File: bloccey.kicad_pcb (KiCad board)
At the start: 2 copper layers, 12 parts

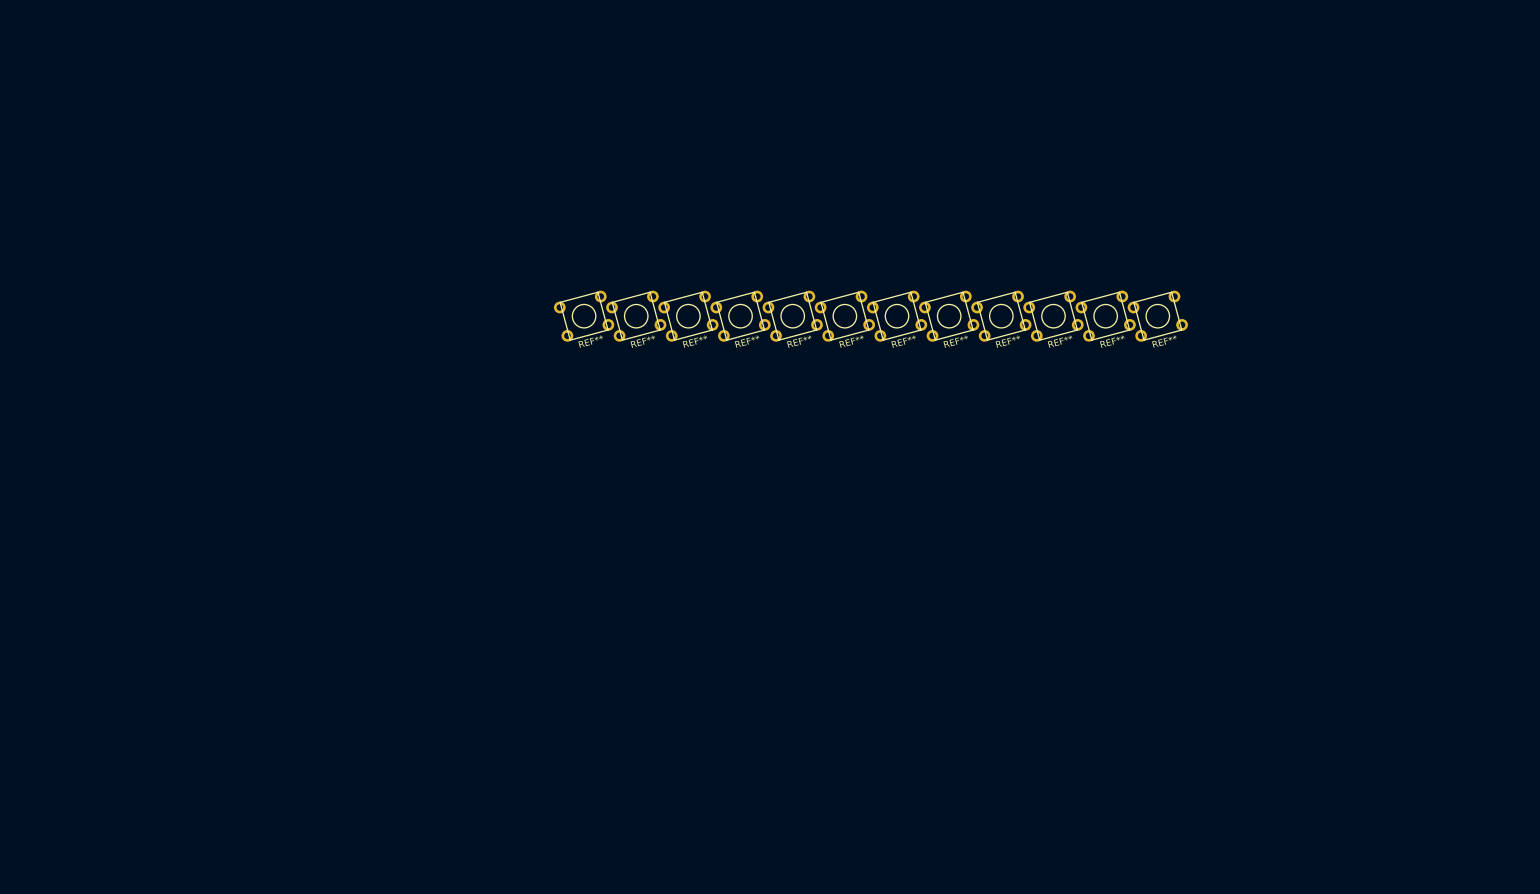
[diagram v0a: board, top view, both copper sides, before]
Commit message: Start of PCB layout, finished sch
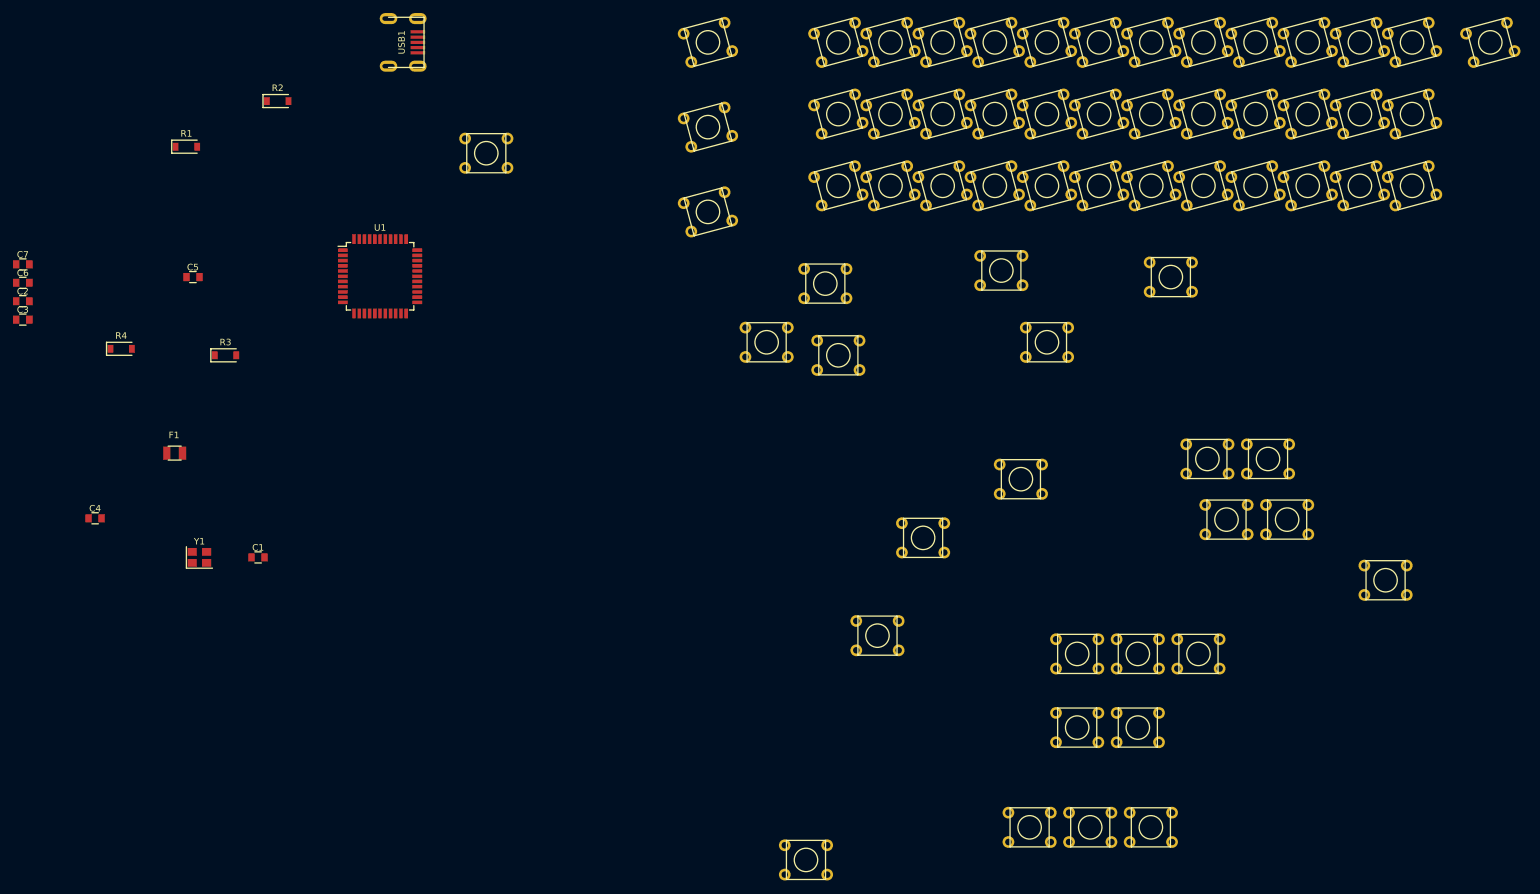
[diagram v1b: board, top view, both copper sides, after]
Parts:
- removed REF** (x12): PushButton_6x6mm_TH, random-keyboard-parts:PushButton_6x6mm_TH
- added C1: 22pF, Capacitors_SMD:C_0805, F.Cu at (61.0, 109.0)
- added C2: 22pF, Capacitors_SMD:C_0805, F.Cu at (24.9, 69.7)
- added C3: 1uF, Capacitors_SMD:C_0805, F.Cu at (24.9, 72.5)
- added C4: 0.1uF, Capacitors_SMD:C_0805, F.Cu at (36.0, 103.0)
- added C5: 0.1uF, Capacitors_SMD:C_0805, F.Cu at (51.0, 66.0)
- added C6: 0.1uF, Capacitors_SMD:C_0805, F.Cu at (24.9, 66.9)
- added C7: 10uF, Capacitors_SMD:C_0805, F.Cu at (24.9, 64.1)
- added F1: 500mA, Fuse_Holders_and_Fuses:Fuse_SMD1206_Reflow, F.Cu at (48.2, 93.0)
- added R1: 10k, random-keyboard-parts:D_SOD-123-Pretty, F.Cu at (50.0, 46.0)
- added R2: 22, random-keyboard-parts:D_SOD-123-Pretty, F.Cu at (64.0, 39.0)
- added R3: 22, random-keyboard-parts:D_SOD-123-Pretty, F.Cu at (56.0, 78.0)
- added R4: 10k, random-keyboard-parts:D_SOD-123-Pretty, F.Cu at (40.0, 77.0)
- added SW1: SW_Push, random-keyboard-parts:PushButton_6x6mm_TH_Pretty, F.Cu at (96.0, 47.0)
- added SW10: SW_Push, random-keyboard-parts:PushButton_6x6mm_TH_Pretty, F.Cu at (206.0, 30.0)
- added SW11: SW_Push, random-keyboard-parts:PushButton_6x6mm_TH_Pretty, F.Cu at (214.0, 30.0)
- added SW12: SW_Push, random-keyboard-parts:PushButton_6x6mm_TH_Pretty, F.Cu at (222.0, 30.0)
- added SW13: SW_Push, random-keyboard-parts:PushButton_6x6mm_TH_Pretty, F.Cu at (230.0, 30.0)
- added SW14: SW_Push, random-keyboard-parts:PushButton_6x6mm_TH_Pretty, F.Cu at (238.0, 30.0)
- added SW15: SW_Push, random-keyboard-parts:PushButton_6x6mm_TH_Pretty, F.Cu at (130.0, 43.0)
- added SW16: SW_Push, random-keyboard-parts:PushButton_6x6mm_TH_Pretty, F.Cu at (150.0, 41.0)
- added SW17: SW_Push, random-keyboard-parts:PushButton_6x6mm_TH_Pretty, F.Cu at (158.0, 41.0)
- added SW18: SW_Push, random-keyboard-parts:PushButton_6x6mm_TH_Pretty, F.Cu at (166.0, 41.0)
- added SW19: SW_Push, random-keyboard-parts:PushButton_6x6mm_TH_Pretty, F.Cu at (174.0, 41.0)
- added SW2: SW_Push, random-keyboard-parts:PushButton_6x6mm_TH_Pretty, F.Cu at (130.0, 30.0)
- added SW20: SW_Push, random-keyboard-parts:PushButton_6x6mm_TH_Pretty, F.Cu at (182.0, 41.0)
- added SW21: SW_Push, random-keyboard-parts:PushButton_6x6mm_TH_Pretty, F.Cu at (190.0, 41.0)
- added SW22: SW_Push, random-keyboard-parts:PushButton_6x6mm_TH_Pretty, F.Cu at (198.0, 41.0)
- added SW23: SW_Push, random-keyboard-parts:PushButton_6x6mm_TH_Pretty, F.Cu at (206.0, 41.0)
- added SW24: SW_Push, random-keyboard-parts:PushButton_6x6mm_TH_Pretty, F.Cu at (214.0, 41.0)
- added SW25: SW_Push, random-keyboard-parts:PushButton_6x6mm_TH_Pretty, F.Cu at (222.0, 41.0)
- added SW26: SW_Push, random-keyboard-parts:PushButton_6x6mm_TH_Pretty, F.Cu at (230.0, 41.0)
- added SW27: SW_Push, random-keyboard-parts:PushButton_6x6mm_TH_Pretty, F.Cu at (238.0, 41.0)
- added SW28: SW_Push, random-keyboard-parts:PushButton_6x6mm_TH_Pretty, F.Cu at (130.0, 56.0)
- added SW29: SW_Push, random-keyboard-parts:PushButton_6x6mm_TH_Pretty, F.Cu at (150.0, 52.0)
- added SW3: SW_Push, random-keyboard-parts:PushButton_6x6mm_TH_Pretty, F.Cu at (150.0, 30.0)
- added SW30: SW_Push, random-keyboard-parts:PushButton_6x6mm_TH_Pretty, F.Cu at (158.0, 52.0)
- added SW31: SW_Push, random-keyboard-parts:PushButton_6x6mm_TH_Pretty, F.Cu at (166.0, 52.0)
- added SW32: SW_Push, random-keyboard-parts:PushButton_6x6mm_TH_Pretty, F.Cu at (174.0, 52.0)
- added SW33: SW_Push, random-keyboard-parts:PushButton_6x6mm_TH_Pretty, F.Cu at (182.0, 52.0)
- added SW34: SW_Push, random-keyboard-parts:PushButton_6x6mm_TH_Pretty, F.Cu at (190.0, 52.0)
- added SW35: SW_Push, random-keyboard-parts:PushButton_6x6mm_TH_Pretty, F.Cu at (198.0, 52.0)
- added SW36: SW_Push, random-keyboard-parts:PushButton_6x6mm_TH_Pretty, F.Cu at (206.0, 52.0)
- added SW37: SW_Push, random-keyboard-parts:PushButton_6x6mm_TH_Pretty, F.Cu at (214.0, 52.0)
- added SW38: SW_Push, random-keyboard-parts:PushButton_6x6mm_TH_Pretty, F.Cu at (222.0, 52.0)
- added SW39: SW_Push, random-keyboard-parts:PushButton_6x6mm_TH_Pretty, F.Cu at (230.0, 52.0)
- added SW4: SW_Push, random-keyboard-parts:PushButton_6x6mm_TH_Pretty, F.Cu at (158.0, 30.0)
- added SW40: SW_Push, random-keyboard-parts:PushButton_6x6mm_TH_Pretty, F.Cu at (238.0, 52.0)
- added SW41: SW_Push, random-keyboard-parts:PushButton_6x6mm_TH_Pretty, F.Cu at (186.6, 123.8)
- added SW42: SW_Push, random-keyboard-parts:PushButton_6x6mm_TH_Pretty, F.Cu at (233.9, 112.5)
- added SW43: SW_Push, random-keyboard-parts:PushButton_6x6mm_TH_Pretty, F.Cu at (148.0, 67.0)
- added SW44: SW_Push, random-keyboard-parts:PushButton_6x6mm_TH_Pretty, F.Cu at (178.0, 97.0)
- added SW45: SW_Push, random-keyboard-parts:PushButton_6x6mm_TH_Pretty, F.Cu at (175.0, 65.0)
- added SW46: SW_Push, random-keyboard-parts:PushButton_6x6mm_TH_Pretty, F.Cu at (179.3, 150.4)
- added SW47: SW_Push, random-keyboard-parts:PushButton_6x6mm_TH_Pretty, F.Cu at (215.9, 93.9)
- added SW48: SW_Push, random-keyboard-parts:PushButton_6x6mm_TH_Pretty, F.Cu at (145.0, 155.4)
- added SW49: SW_Push, random-keyboard-parts:PushButton_6x6mm_TH_Pretty, F.Cu at (201.0, 66.0)
- added SW5: SW_Push, random-keyboard-parts:PushButton_6x6mm_TH_Pretty, F.Cu at (166.0, 30.0)
- added SW50: SW_Push, random-keyboard-parts:PushButton_6x6mm_TH_Pretty, F.Cu at (163.0, 106.0)
- added SW51: SW_Push, random-keyboard-parts:PushButton_6x6mm_TH_Pretty, F.Cu at (156.0, 121.0)
- added SW52: SW_Push, random-keyboard-parts:PushButton_6x6mm_TH_Pretty, F.Cu at (195.9, 123.8)
- added SW53: SW_Push, random-keyboard-parts:PushButton_6x6mm_TH_Pretty, F.Cu at (206.6, 93.9)
- added SW54: SW_Push, random-keyboard-parts:PushButton_6x6mm_TH_Pretty, F.Cu at (139.0, 76.0)
- added SW55: SW_Push, random-keyboard-parts:PushButton_6x6mm_TH_Pretty, F.Cu at (150.0, 78.0)
- added SW56: SW_Push, random-keyboard-parts:PushButton_6x6mm_TH_Pretty, F.Cu at (209.5, 103.2)
- added SW57: SW_Push, random-keyboard-parts:PushButton_6x6mm_TH_Pretty, F.Cu at (188.6, 150.4)
- added SW58: SW_Push, random-keyboard-parts:PushButton_6x6mm_TH_Pretty, F.Cu at (182.0, 76.0)
- added SW59: SW_Push, random-keyboard-parts:PushButton_6x6mm_TH_Pretty, F.Cu at (195.9, 135.1)
- added SW6: SW_Push, random-keyboard-parts:PushButton_6x6mm_TH_Pretty, F.Cu at (174.0, 30.0)
- added SW60: SW_Push, random-keyboard-parts:PushButton_6x6mm_TH_Pretty, F.Cu at (205.2, 123.8)
- added SW61: SW_Push, random-keyboard-parts:PushButton_6x6mm_TH_Pretty, F.Cu at (250.0, 30.0)
- added SW62: SW_Push, random-keyboard-parts:PushButton_6x6mm_TH_Pretty, F.Cu at (218.8, 103.2)
- added SW63: SW_Push, random-keyboard-parts:PushButton_6x6mm_TH_Pretty, F.Cu at (186.6, 135.1)
- added SW64: SW_Push, random-keyboard-parts:PushButton_6x6mm_TH_Pretty, F.Cu at (197.9, 150.4)
- added SW7: SW_Push, random-keyboard-parts:PushButton_6x6mm_TH_Pretty, F.Cu at (182.0, 30.0)
- added SW8: SW_Push, random-keyboard-parts:PushButton_6x6mm_TH_Pretty, F.Cu at (190.0, 30.0)
- added SW9: SW_Push, random-keyboard-parts:PushButton_6x6mm_TH_Pretty, F.Cu at (198.0, 30.0)
- added U1: ATmega32U4-AU, Housings_QFP:TQFP-44_10x10mm_Pitch0.8mm, F.Cu at (79.7, 65.9)
- added USB1: Molex-0548190589, random-keyboard-parts:Molex-0548190589, F.Cu at (81.0, 30.0)
- added Y1: 16MHz, Crystals:Crystal_SMD_3225-4pin_3.2x2.5mm, F.Cu at (52.0, 109.0)

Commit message: Updated switch positions
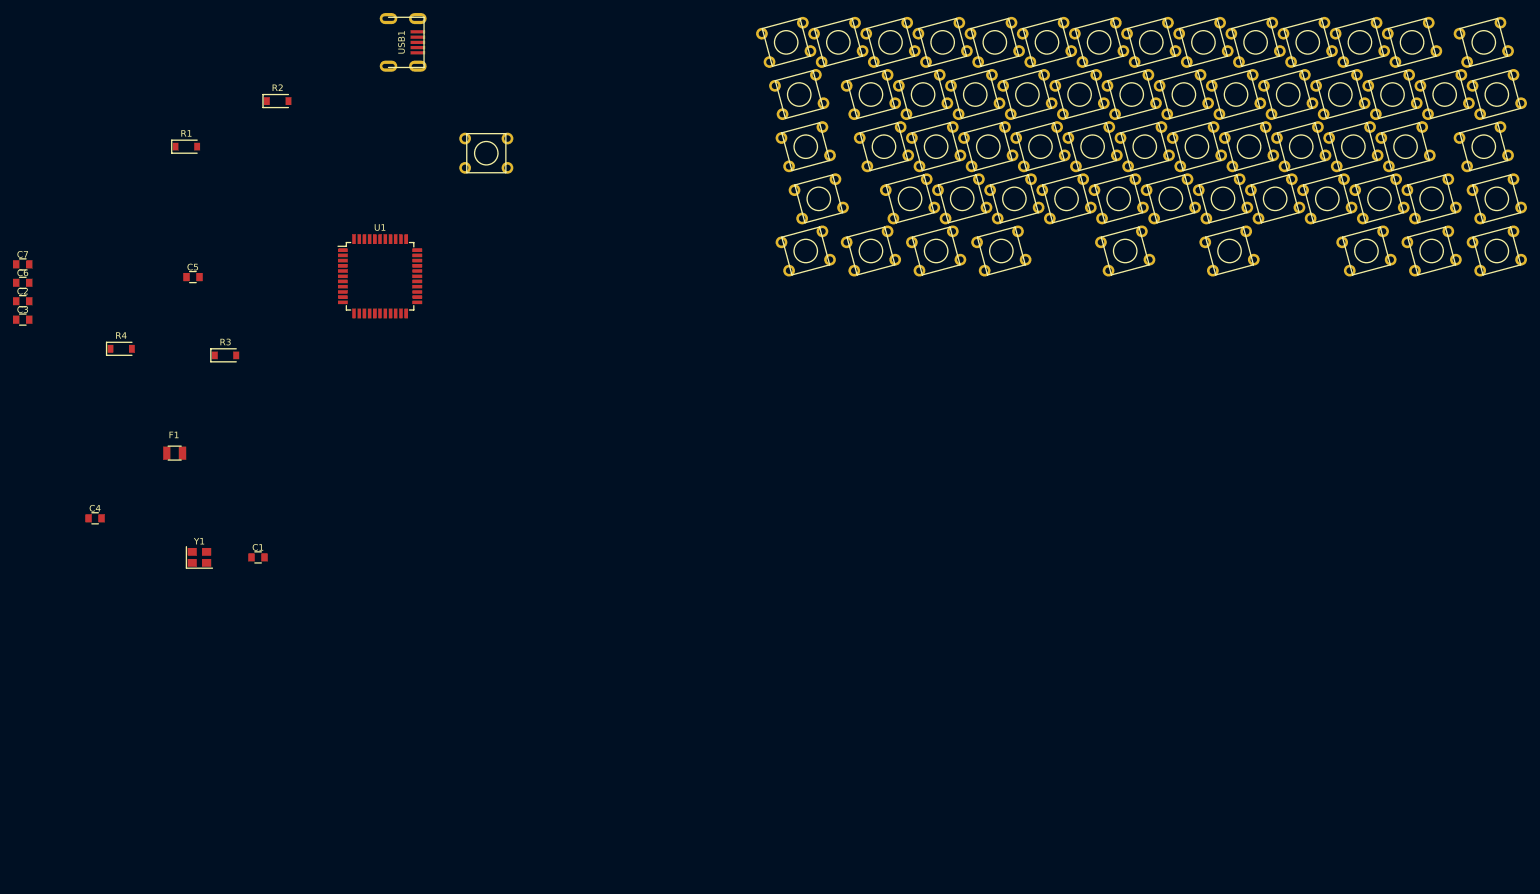
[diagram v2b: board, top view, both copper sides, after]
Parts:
- moved SW48 119.9 mm to (209.0, 54.0), turned to 15 degrees
- moved SW60 103.5 mm to (249.0, 30.0), turned to 15 degrees
- moved SW64 103.1 mm to (251.0, 62.0), turned to 15 degrees
- moved SW51 102.1 mm to (233.0, 54.0), turned to 15 degrees
- moved SW46 97.4 mm to (193.0, 54.0), turned to 15 degrees
- moved SW42 93.5 mm to (161.0, 54.0), turned to 15 degrees
- moved SW63 91.1 mm to (241.0, 62.0), turned to 15 degrees
- moved SW57 89.4 mm to (175.0, 62.0), turned to 15 degrees
- moved SW52 83.1 mm to (241.0, 54.0), turned to 15 degrees
- moved SW50 80.9 mm to (225.0, 54.0), turned to 15 degrees
- moved SW41 80.3 mm to (147.0, 54.0), turned to 15 degrees
- moved SW59 74.4 mm to (210.0, 62.0), turned to 15 degrees
- moved SW56 60.7 mm to (165.0, 62.0), turned to 15 degrees
- moved SW53 59.7 mm to (251.0, 54.0), turned to 15 degrees
- moved SW44 43.0 mm to (177.0, 54.0), turned to 15 degrees
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
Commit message: Switch to STM32, redo PCB
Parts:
- removed C1, C2: 22pF, Capacitors_SMD:C_0805
- removed C3: 1uF, Capacitors_SMD:C_0805
- removed C4, C5, C6: 0.1uF, Capacitors_SMD:C_0805
- removed C7: 10uF, Capacitors_SMD:C_0805
- removed F1: 500mA, Fuse_Holders_and_Fuses:Fuse_SMD1206_Reflow
- removed R1, R4: 10k, random-keyboard-parts:D_SOD-123-Pretty
- removed R2, R3: 22, random-keyboard-parts:D_SOD-123-Pretty
- removed SW1: SW_Push, random-keyboard-parts:PushButton_6x6mm_TH_Pretty
- removed U1: ATmega32U4-AU, Housings_QFP:TQFP-44_10x10mm_Pitch0.8mm
- removed USB1: Molex-0548190589, random-keyboard-parts:Molex-0548190589
- removed Y1: 16MHz, Crystals:Crystal_SMD_3225-4pin_3.2x2.5mm
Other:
- net class Default: trace_width 0.25 -> 0.254
- net class Power added: clearance 0.2, trace_width 0.381, via_dia 0.8, via_drill 0.4
